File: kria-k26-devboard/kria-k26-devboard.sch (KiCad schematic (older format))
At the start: 2 parts

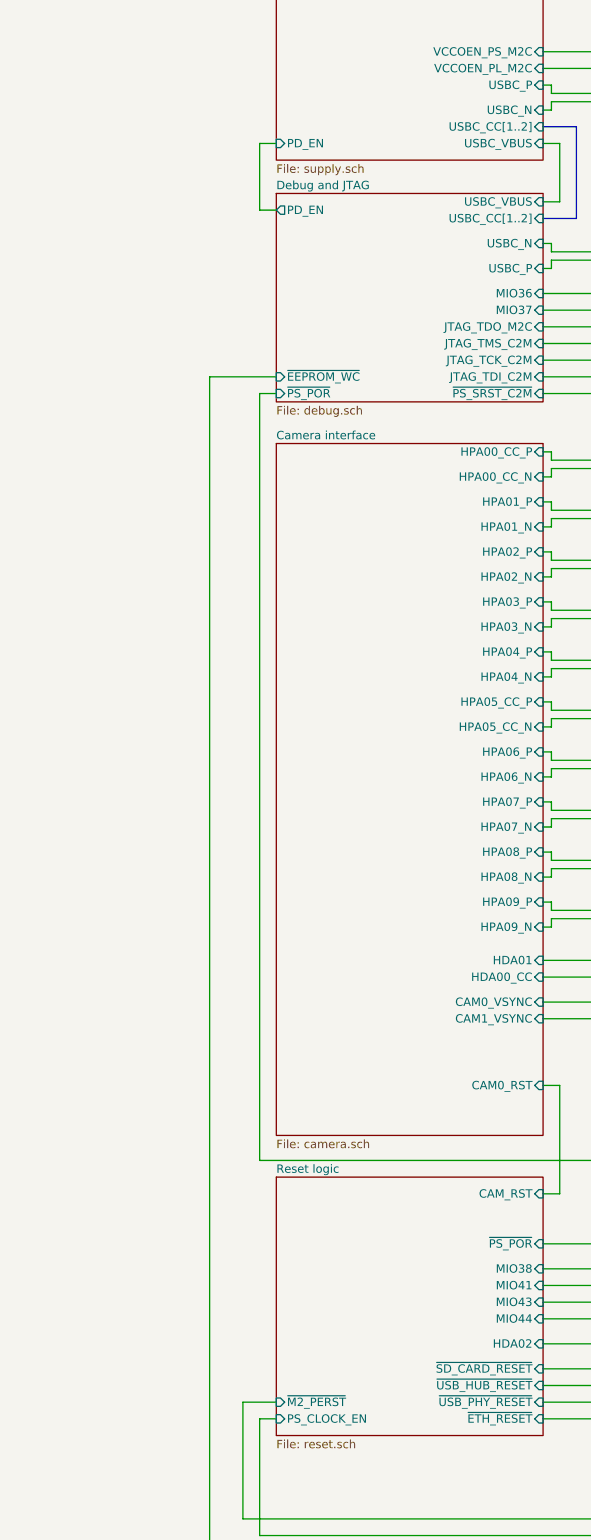
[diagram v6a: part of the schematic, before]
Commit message: Finished Power planes and overall connectivity
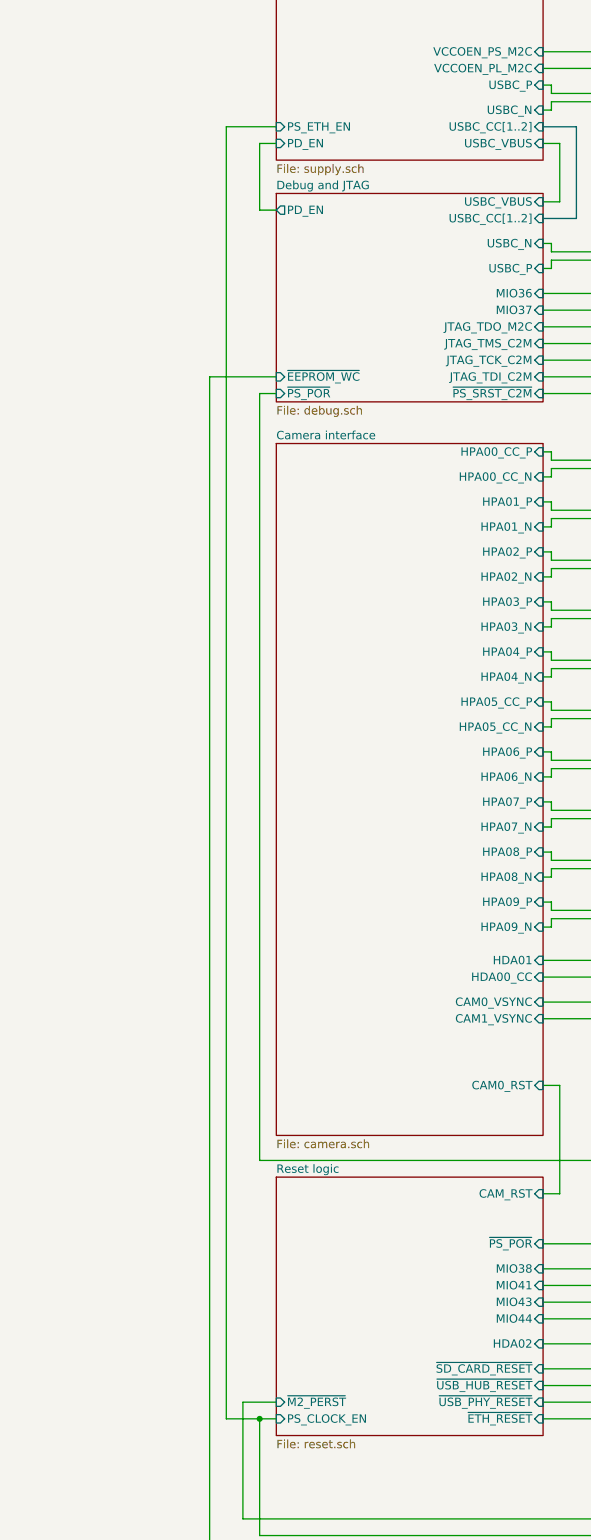
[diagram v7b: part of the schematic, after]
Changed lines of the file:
@@
 F8 "USBC_VBUS" I R 5950 1650 50
 F9 "PD_EN" I L 4350 1650 50
+F10 "PS_ETH_EN" I L 4350 1550 50
 $EndSheet
 Wire Wire Line
@@
 	1    0    0    -1
 $EndComp
+Wire Wire Line
+	4250 9300 4050 9300
+Wire Wire Line
+	4050 9300 4050 1550
+Wire Wire Line
+	4050 1550 4350 1550
+Connection ~ 4250 9300
 $EndSCHEMATC

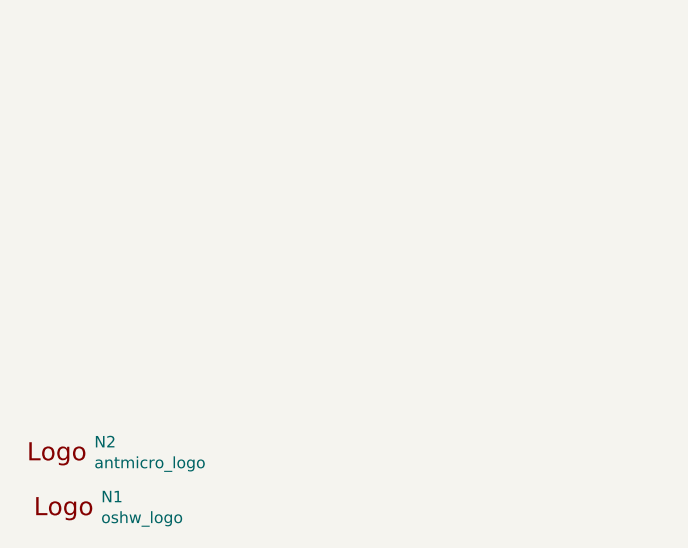
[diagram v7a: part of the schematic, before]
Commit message: Optimization of power planes, fixed missing capacitors on USB 3.0, unify shields, polishing of layout
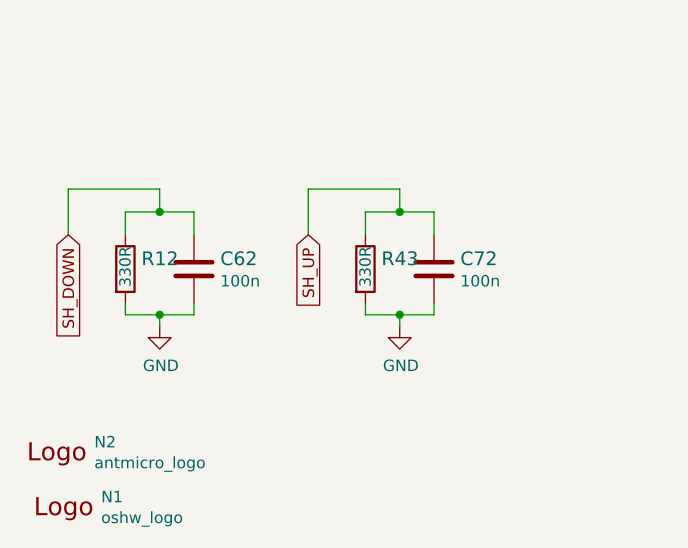
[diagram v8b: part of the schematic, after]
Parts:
- added C62, C72: C_100n_0402, antmicro-footprints:0402-cap, symbol antmicroCapacitors0402:C_100n_0402
- added R12, R43: R_330R_0402, antmicro-footprints:0402-res, symbol antmicroResistors0402:R_330R_0402
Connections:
- new net GND: C62.2, C72.2, R12.2, R43.2
- new net SH_DOWN: C62.1, R12.1
- new net SH_UP: C72.1, R43.1
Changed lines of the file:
@@
 	4050 1550 4350 1550
 Connection ~ 4250 9300
+$Comp
+L antmicroResistors0402:R_330R_0402 R?
+U 1 1 62A3B8DC
+P 1000 10000
+AR Path="/63CADD16/62A3B8DC" Ref="R?"  Part="1"
+AR Path="/625B0244/62A3B8DC" Ref="R?"  Part="1"
+AR Path="/63C44BC2/62A9ECDC/62A3B8DC" Ref="R?"  Part="1"
+AR Path="/62A3B8DC" Ref="R12"  Part="1"
+F 0 "R12" V 955 10070 60  0000 L CNN
+F 1 "R_330R_0402" H 1000 9850 60  0001 C CNN
+F 2 "antmicro-footprints:0402-res" H 1200 10200 60  0001 L CNN
+F 3 "" H 1000 10000 50  0001 C CNN
+F 4 "MULTICOMP" H 1200 10400 60  0001 L CNN "Manufacturer"
+F 5 "MCMR04X3300FTL" H 1200 10300 60  0001 L CNN "MPN"
+F 6 "330R" H 900 10000 50  0000 L CNN "Val"
+	1    1000 10000
+	0    1    1    0
+$EndComp
+$Comp
+L antmicroCapacitors0402:C_100n_0402 C?
+U 1 1 62A3B8E5
+P 1300 10000
+AR Path="/63CADD16/62A3B8E5" Ref="C?"  Part="1"
+AR Path="/625B0244/62A3B8E5" Ref="C?"  Part="1"
+AR Path="/63C44BC2/62A9ECDC/62A3B8E5" Ref="C?"  Part="1"
+AR Path="/62A3B8E5" Ref="C62"  Part="1"
+F 0 "C62" H 1415 10045 60  0000 L CNN
+F 1 "C_100n_0402" H 1300 9850 60  0001 C CNN
+F 2 "antmicro-footprints:0402-cap" H 1500 10200 60  0001 L CNN
+F 3 "" H 1300 10000 50  0001 C CNN
+F 4 "Murata" H 1500 10400 60  0001 L CNN "Manufacturer"
+F 5 "GRM155R61H104KE14D" H 1500 10300 60  0001 L CNN "MPN"
+F 6 "100n" H 1415 9947 50  0000 L CNN "Val"
+	1    1300 10000
+	1    0    0    -1
+$EndComp
+Wire Wire Line
+	1000 10150 1000 10200
+Wire Wire Line
+	1000 10200 1150 10200
+Wire Wire Line
+	1150 10250 1150 10200
+Connection ~ 1150 10200
+Wire Wire Line
+	1150 10200 1300 10200
+Wire Wire Line
+	1300 10200 1300 10150
+$Comp
+L power:GND #PWR?
+U 1 1 62A3B8F1
+P 1150 10250
+AR Path="/63CADD16/62A3B8F1" Ref="#PWR?"  Part="1"
+AR Path="/625B0244/62A3B8F1" Ref="#PWR?"  Part="1"
+AR Path="/63C44BC2/62A9ECDC/62A3B8F1" Ref="#PWR?"  Part="1"
+AR Path="/62A3B8F1" Ref="#PWR0101"  Part="1"
+F 0 "#PWR0101" H 1150 10000 50  0001 C CNN
+F 1 "GND" H 1155 10077 50  0000 C CNN
+F 2 "" H 1150 10250 50  0001 C CNN
+F 3 "" H 1150 10250 50  0001 C CNN
+	1    1150 10250
+	1    0    0    -1
+$EndComp
+Wire Wire Line
+	1300 9750 1300 9850
+Wire Wire Line
+	1000 9850 1000 9750
+Wire Wire Line
+	1000 9750 1150 9750
+Wire Wire Line
+	1150 9750 1150 9650
+Wire Wire Line
+	1150 9650 750  9650
+Connection ~ 1150 9750
+Wire Wire Line
+	1150 9750 1300 9750
+Wire Wire Line
+	750  9650 750  9850
+$Comp
+L antmicroResistors0402:R_330R_0402 R?
+U 1 1 62B170E5
+P 2050 10000
+AR Path="/63CADD16/62B170E5" Ref="R?"  Part="1"
+AR Path="/625B0244/62B170E5" Ref="R?"  Part="1"
+AR Path="/63C44BC2/62A9ECDC/62B170E5" Ref="R?"  Part="1"
+AR Path="/62B170E5" Ref="R43"  Part="1"
+F 0 "R43" V 2005 10070 60  0000 L CNN
+F 1 "R_330R_0402" H 2050 9850 60  0001 C CNN
+F 2 "antmicro-footprints:0402-res" H 2250 10200 60  0001 L CNN
+F 3 "" H 2050 10000 50  0001 C CNN
+F 4 "MULTICOMP" H 2250 10400 60  0001 L CNN "Manufacturer"
+F 5 "MCMR04X3300FTL" H 2250 10300 60  0001 L CNN "MPN"
+F 6 "330R" H 1950 10000 50  0000 L CNN "Val"
+	1    2050 10000
+	0    1    1    0
+$EndComp
+$Comp
+L antmicroCapacitors0402:C_100n_0402 C?
+U 1 1 62B17134
+P 2350 10000
+AR Path="/63CADD16/62B17134" Ref="C?"  Part="1"
+AR Path="/625B0244/62B17134" Ref="C?"  Part="1"
+AR Path="/63C44BC2/62A9ECDC/62B17134" Ref="C?"  Part="1"
+AR Path="/62B17134" Ref="C72"  Part="1"
+F 0 "C72" H 2465 10045 60  0000 L CNN
+F 1 "C_100n_0402" H 2350 9850 60  0001 C CNN
+F 2 "antmicro-footprints:0402-cap" H 2550 10200 60  0001 L CNN
+F 3 "" H 2350 10000 50  0001 C CNN
+F 4 "Murata" H 2550 10400 60  0001 L CNN "Manufacturer"
+F 5 "GRM155R61H104KE14D" H 2550 10300 60  0001 L CNN "MPN"
+F 6 "100n" H 2465 9947 50  0000 L CNN "Val"
+	1    2350 10000
+	1    0    0    -1
+$EndComp
+Wire Wire Line
+	2050 10150 2050 10200
+Wire Wire Line
+	2050 10200 2200 10200
+Wire Wire Line
+	2200 10250 2200 10200
+Connection ~ 2200 10200
+Wire Wire Line
+	2200 10200 2350 10200
+Wire Wire Line
+	2350 10200 2350 10150
+$Comp
+L power:GND #PWR?
+U 1 1 62B17144
+P 2200 10250
+AR Path="/63CADD16/62B17144" Ref="#PWR?"  Part="1"
+AR Path="/625B0244/62B17144" Ref="#PWR?"  Part="1"
+AR Path="/63C44BC2/62A9ECDC/62B17144" Ref="#PWR?"  Part="1"
+AR Path="/62B17144" Ref="#PWR0366"  Part="1"
+F 0 "#PWR0366" H 2200 10000 50  0001 C CNN
+F 1 "GND" H 2205 10077 50  0000 C CNN
+F 2 "" H 2200 10250 50  0001 C CNN
+F 3 "" H 2200 10250 50  0001 C CNN
+	1    2200 10250
+	1    0    0    -1
+$EndComp
+Wire Wire Line
+	2350 9750 2350 9850
+Wire Wire Line
+	2050 9850 2050 9750
+Wire Wire Line
+	2050 9750 2200 9750
+Wire Wire Line
+	2200 9750 2200 9650
+Wire Wire Line
+	2200 9650 1800 9650
+Connection ~ 2200 9750
+Wire Wire Line
+	2200 9750 2350 9750
+Wire Wire Line
+	1800 9650 1800 9850
+Text GLabel 750  9850 3    50   Input ~ 0
+SH_DOWN
+Text GLabel 1800 9850 3    50   Input ~ 0
+SH_UP
 $EndSCHEMATC
